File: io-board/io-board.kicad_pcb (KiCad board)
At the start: 2 copper layers, 82 x 64 mm, 101 parts, among them J1 Conn_01x03, J2 Conn_01x03, J3 Conn_01x03, J4 Conn_01x03, J5 Conn_01x24, K1 FRM18A-5 DC12V, K10 FRM18A-5 DC12V, K11 FRM18A-5 DC12V, K2 FRM18A-5 DC12V, K3 FRM18A-5 DC12V, K4 FRM18A-5 DC12V, K5 FRM18A-5 DC12V, K6 FRM18A-5 DC12V, K7 FRM18A-5 DC12V, K8 FRM18A-5 DC12V, K9 FRM18A-5 DC12V, Q1 NPN, Q10 NPN, Q11 NPN, Q2 NPN, Q3 NPN, Q4 NPN, Q5 NPN, Q6 NPN, Q7 NPN, Q8 NPN, Q9 NPN, U1 Littelfuse SP720, U2 Kamod BluePill STM32F103C8T6

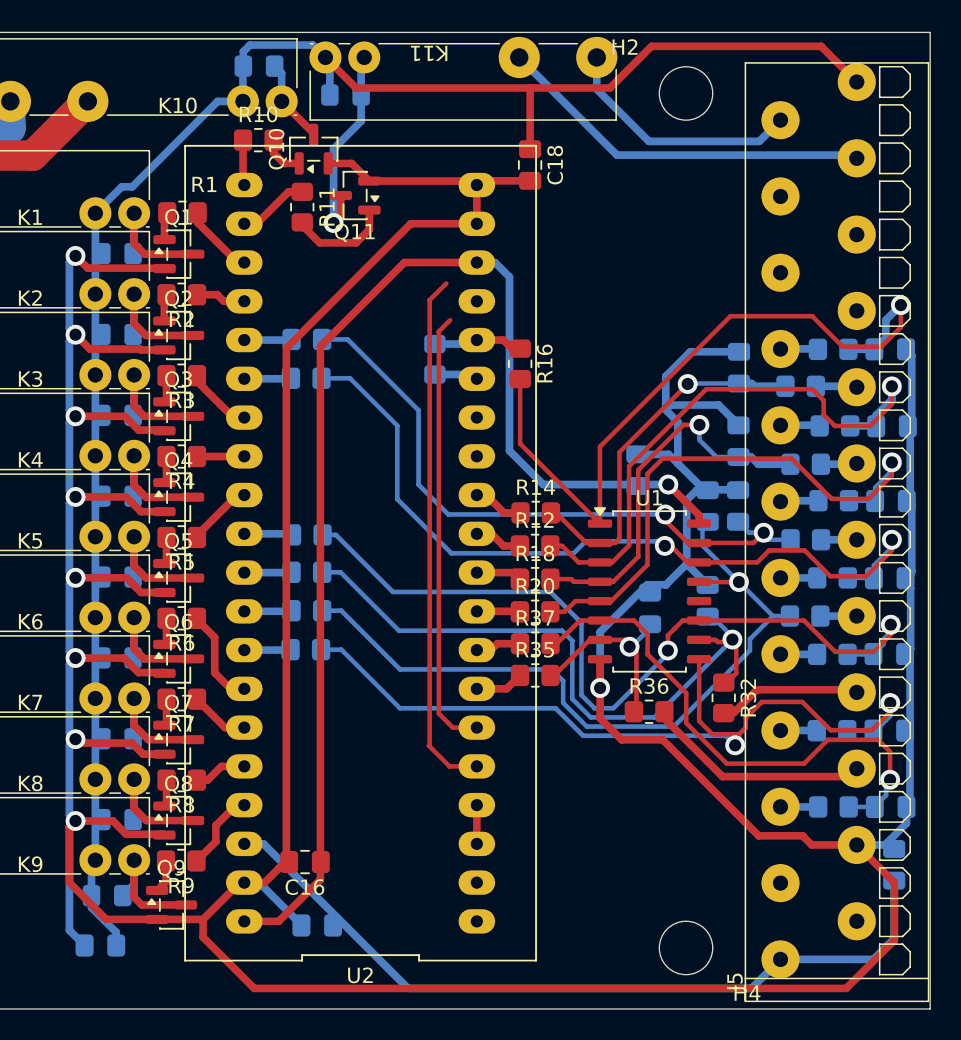
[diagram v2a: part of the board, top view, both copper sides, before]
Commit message: All added and connected in PCB. Cleanup needed.
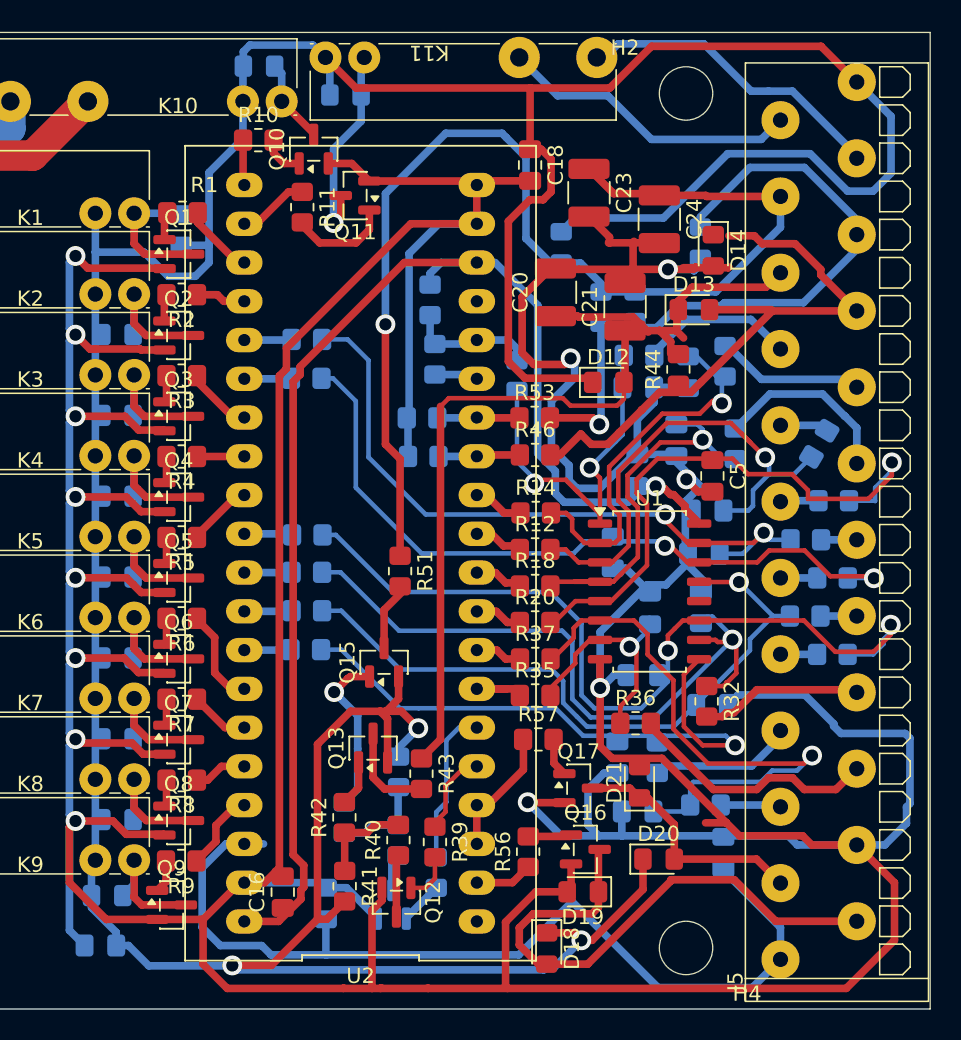
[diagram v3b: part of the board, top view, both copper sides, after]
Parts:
- added C20: C, Capacitor_SMD:C_1210_3225Metric_Pad1.33x2.70mm_HandSolder, F.Cu at (87.4, 47.0)
- added C21: C, Capacitor_SMD:C_1210_3225Metric_Pad1.33x2.70mm_HandSolder, F.Cu at (92.0, 48.0)
- added C23: C, Capacitor_SMD:C_1210_3225Metric_Pad1.33x2.70mm_HandSolder, F.Cu at (89.6, 40.5)
- added C24: C, Capacitor_SMD:C_1210_3225Metric_Pad1.33x2.70mm_HandSolder, F.Cu at (94.2, 42.2)
- added D12: D, Diode_SMD:D_0805_2012Metric_Pad1.15x1.40mm_HandSolder, F.Cu at (90.9, 52.9)
- added D13: D, Diode_SMD:D_0805_2012Metric_Pad1.15x1.40mm_HandSolder, F.Cu at (96.5, 48.2)
- added D14: D, Diode_SMD:D_0805_2012Metric_Pad1.15x1.40mm_HandSolder, F.Cu at (97.8, 44.3)
- added D15: D, Diode_SMD:D_0805_2012Metric_Pad1.15x1.40mm_HandSolder, B.Cu at (87.8, 44.1)
- added D16: D, Diode_SMD:D_0805_2012Metric_Pad1.15x1.40mm_HandSolder, B.Cu at (90.4, 48.0)
- added D17: D, Diode_SMD:D_0805_2012Metric_Pad1.15x1.40mm_HandSolder, B.Cu at (96.9, 43.8)
- added D18: D, Diode_SMD:D_0805_2012Metric_Pad1.15x1.40mm_HandSolder, F.Cu at (86.9, 90.0)
- added D19: D, Diode_SMD:D_0805_2012Metric_Pad1.15x1.40mm_HandSolder, F.Cu at (89.2, 86.3)
- added D20: D, Diode_SMD:D_0805_2012Metric_Pad1.15x1.40mm_HandSolder, F.Cu at (94.2, 84.2)
- added D21: D, Diode_SMD:D_0805_2012Metric_Pad1.15x1.40mm_HandSolder, F.Cu at (93.0, 79.1)
- added Q12: NPN, Package_TO_SOT_SMD:SOT-23, F.Cu at (77.0, 87.0)
- added Q13: PNP, Package_TO_SOT_SMD:SOT-23, F.Cu at (75.5, 76.9)
- added Q14: NPN, Package_TO_SOT_SMD:SOT-23, B.Cu at (76.7, 87.1)
- added Q15: PNP, Package_TO_SOT_SMD:SOT-23, F.Cu at (76.2, 71.3)
- added Q16: NPN, Package_TO_SOT_SMD:SOT-23, F.Cu at (89.4, 83.5)
- added Q17: NPN, Package_TO_SOT_SMD:SOT-23, F.Cu at (89.0, 79.5)
- added R39: R, Resistor_SMD:R_0805_2012Metric_Pad1.20x1.40mm_HandSolder, F.Cu at (79.5, 83.1)
- added R40: R, Resistor_SMD:R_0805_2012Metric_Pad1.20x1.40mm_HandSolder, F.Cu at (77.2, 82.9)
- added R41: R, Resistor_SMD:R_0805_2012Metric_Pad1.20x1.40mm_HandSolder, F.Cu at (73.6, 86.0)
- added R42: R, Resistor_SMD:R_0805_2012Metric_Pad1.20x1.40mm_HandSolder, F.Cu at (73.6, 81.4)
- added R43: R, Resistor_SMD:R_0805_2012Metric_Pad1.20x1.40mm_HandSolder, F.Cu at (78.7, 78.6)
- added R44: R, Resistor_SMD:R_0805_2012Metric_Pad1.20x1.40mm_HandSolder, F.Cu at (95.5, 52.1)
- added R45: R, Resistor_SMD:R_0805_2012Metric_Pad1.20x1.40mm_HandSolder, B.Cu at (78.8, 57.8)
- added R46: R, Resistor_SMD:R_0805_2012Metric_Pad1.20x1.40mm_HandSolder, F.Cu at (86.1, 57.7)
- added R47: R, Resistor_SMD:R_0805_2012Metric_Pad1.20x1.40mm_HandSolder, B.Cu at (79.6, 85.1)
- added R48: R, Resistor_SMD:R_0805_2012Metric_Pad1.20x1.40mm_HandSolder, B.Cu at (77.2, 78.5)
- added R49: R, Resistor_SMD:R_0805_2012Metric_Pad1.20x1.40mm_HandSolder, B.Cu at (77.1, 83.0)
- added R50: R, Resistor_SMD:R_0805_2012Metric_Pad1.20x1.40mm_HandSolder, B.Cu at (73.6, 81.5)
- added R51: R, Resistor_SMD:R_0805_2012Metric_Pad1.20x1.40mm_HandSolder, F.Cu at (77.3, 65.3)
- added R52: R, Resistor_SMD:R_0805_2012Metric_Pad1.20x1.40mm_HandSolder, B.Cu at (92.7, 48.0)
- added R53: R, Resistor_SMD:R_0805_2012Metric_Pad1.20x1.40mm_HandSolder, F.Cu at (86.1, 55.3)
- added R54: R, Resistor_SMD:R_0805_2012Metric_Pad1.20x1.40mm_HandSolder, B.Cu at (78.7, 55.3)
- added R55: 50K, Resistor_SMD:R_0805_2012Metric_Pad1.20x1.40mm_HandSolder, B.Cu at (79.2, 47.5)
- added R56: R, Resistor_SMD:R_0805_2012Metric_Pad1.20x1.40mm_HandSolder, F.Cu at (85.7, 83.7)
- added R57: R, Resistor_SMD:R_0805_2012Metric_Pad1.20x1.40mm_HandSolder, F.Cu at (86.3, 76.3)
- C5: moved to F.Cu
- R16: moved to B.Cu
- moved C7 18.2 mm to (91.2, 64.1), turned to -90 degrees
- moved C11 17.9 mm to (91.5, 77.5), turned to -90 degrees
- moved C1 16.7 mm to (92.9, 53.3)
- moved C13 16.6 mm to (92.8, 81.1), turned to 180 degrees
- moved C9 16.2 mm to (93.1, 72.1), turned to 180 degrees
- moved C3 13.3 mm to (97.4, 61.3), turned to 180 degrees
- moved C8 13.0 mm to (97.7, 74.1), turned to 0 degrees
- moved R17 12.7 mm to (92.9, 51.2), turned to 0 degrees
- moved C5 11.8 mm to (97.7, 59.1), turned to -90 degrees
- moved R34 11.6 mm to (94.1, 77.5), turned to -90 degrees
- moved C17 11.2 mm to (98.4, 83.8)
- moved R38 8.39 mm to (97.3, 80.6), turned to 0 degrees
- moved R15 5.21 mm to (98.6, 51.6), turned to 90 degrees
- moved R19 4.80 mm to (99.2, 57.0), turned to 90 degrees
- moved D1 4.46 mm to (62.9, 42.9), turned to 90 degrees
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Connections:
- net Net-(U2-Pin_3) renamed /OC2-IN
- J5 pad 18: /LED1-P -> /LED1-M
- J5 pad 19: /LED1-M -> /LED1-P
- J5 pad 20: /LED2-P -> /LED2-M
- J5 pad 21: /LED2-M -> /LED2-P
- J5 pad 22: REL11-OUT2 -> REL11-OUT1
- J5 pad 23: REL11-OUT1 -> REL11-OUT2
- U2 pad 13: unconnected-(U2-Pin_13-Pad13) -> /LED1-FB
- U2 pad 14: unconnected-(U2-Pin_14-Pad14) -> /LED2-FB
- U2 pad 2: unconnected-(U2-Pin_2-Pad2) -> /OC1-IN
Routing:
- net +12V: track 115.0 -> 257.8 mm, vias 0 -> 3
- net GND: track 350.6 -> 456.6 mm, vias 9 -> 13
- net /LED2-P: track 0.00 -> 75.9 mm, vias 0 -> 1
- net /LED1-P: track 0.00 -> 63.7 mm
- net /LED2-M: track 0.00 -> 45.6 mm, vias 0 -> 1
- net /LED1-M: track 0.00 -> 39.4 mm
- net /OC1: track 0.00 -> 36.8 mm
- net /LED1-PWM: track 34.5 -> 5.14 mm
- net /ESD1: track 48.1 -> 24.2 mm, vias 1 -> 2
- net /LED2-PWM: track 29.0 -> 10.3 mm
- net /OC2: track 0.00 -> 16.2 mm
- net /ESD8: track 54.8 -> 38.8 mm, vias 2 -> 1
- net Net-(Q15-B): track 0.00 -> 11.0 mm, vias 0 -> 1
- net +5V: track 51.7 -> 61.6 mm
- net /IO3: track 2.37 -> 12.2 mm
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
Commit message: PCB: All component locations done
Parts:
- moved K11 18.4 mm to (90.6, 34.5), turned to 0 degrees
- moved D11 13.1 mm to (86.4, 37.2), turned to 180 degrees
- moved C17 11.5 mm to (87.0, 85.3)
- moved C16 7.69 mm to (63.0, 90.3), turned to 180 degrees
- moved D19 6.64 mm to (84.8, 91.2)
- moved Q11 6.41 mm to (75.5, 47.0)
- moved Q10 6.39 mm to (76.9, 41.2)
- moved R11 6.33 mm to (70.7, 47.8)
- moved C14 6.03 mm to (87.2, 56.4), turned to 0 degrees
- moved R33 5.13 mm to (71.5, 75.6)
- moved D10 5.06 mm to (68.3, 37.3)
- moved R51 4.91 mm to (73.9, 61.7)
- moved D3 4.91 mm to (63.3, 53.2), turned to 90 degrees
- moved D2 4.87 mm to (63.3, 48.1), turned to -90 degrees
- moved D4 4.86 mm to (63.3, 58.7), turned to 90 degrees
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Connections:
- U2 pad 22: REL11-IN -> REL1-IN
- U2 pad 23: REL1-IN -> REL11-IN
- U2 pad 26: /IO-IN6 -> REL3-IN
- U2 pad 27: REL3-IN -> /IO-IN6
- U2 pad 29: REL5-IN -> /IO-IN8
- U2 pad 30: /IO-IN8 -> REL5-IN
- U2 pad 32: /IO-IN7 -> REL6-IN
- U2 pad 33: /IO-IN10 -> /IO-IN7
- U2 pad 34: REL6-IN -> REL7-IN
- U2 pad 35: REL7-IN -> /IO-IN10
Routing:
- net +12V: track 257.8 -> 275.8 mm
- net REL11-OUT1: track 21.3 -> 39.0 mm
- net Net-(D11-A): track 13.7 -> 26.7 mm
- net REL11-OUT2: track 19.9 -> 30.7 mm
- net Net-(D10-A): track 5.56 -> 13.6 mm
- net Net-(R40-Pad2): track 6.27 -> 13.0 mm
- net /LED2-M: track 45.6 -> 51.4 mm
- net +5V: track 61.6 -> 56.2 mm
- net /ESD13: track 47.4 -> 43.3 mm
- net /ESD8: track 38.8 -> 42.8 mm
- net /ESD9: track 44.9 -> 41.0 mm
- net /ESD12: track 43.9 -> 40.7 mm
- net REL6-IN: track 6.43 -> 3.29 mm
- net /LED1-P: track 63.7 -> 60.6 mm
- net Net-(Q9-B): track 2.17 -> 5.01 mm
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
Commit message: PCB: All in place, need to prepare for production
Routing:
- net GND: track 456.9 -> 475.9 mm, vias 13 -> 14
- net /ESD5: track 38.7 -> 32.8 mm
- net /LED2-P: track 75.4 -> 80.3 mm
- net /ESD10: track 53.3 -> 48.7 mm
- net /LED1-P: track 60.6 -> 63.5 mm
- net /ESD13: track 43.3 -> 44.9 mm
- net /ESD3: track 32.4 -> 31.1 mm
- net /IO11: track 16.3 -> 15.1 mm
- net /ESD6: track 37.8 -> 39.1 mm
- net REL9-IN: track 5.27 -> 5.89 mm
- added copper zone on B.Cu, net GND
- added copper zone on F.Cu, net GND

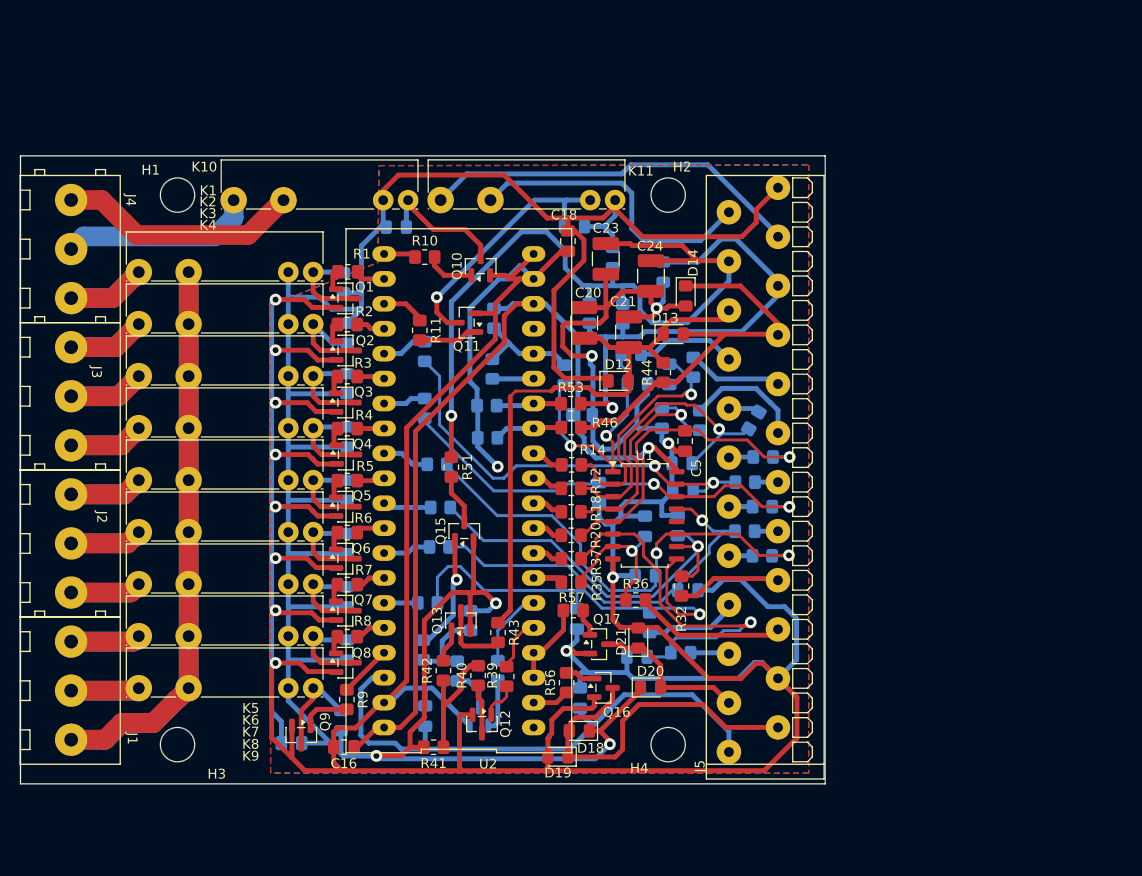
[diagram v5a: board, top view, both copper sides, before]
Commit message: PCB: Stencil holders and production configuration
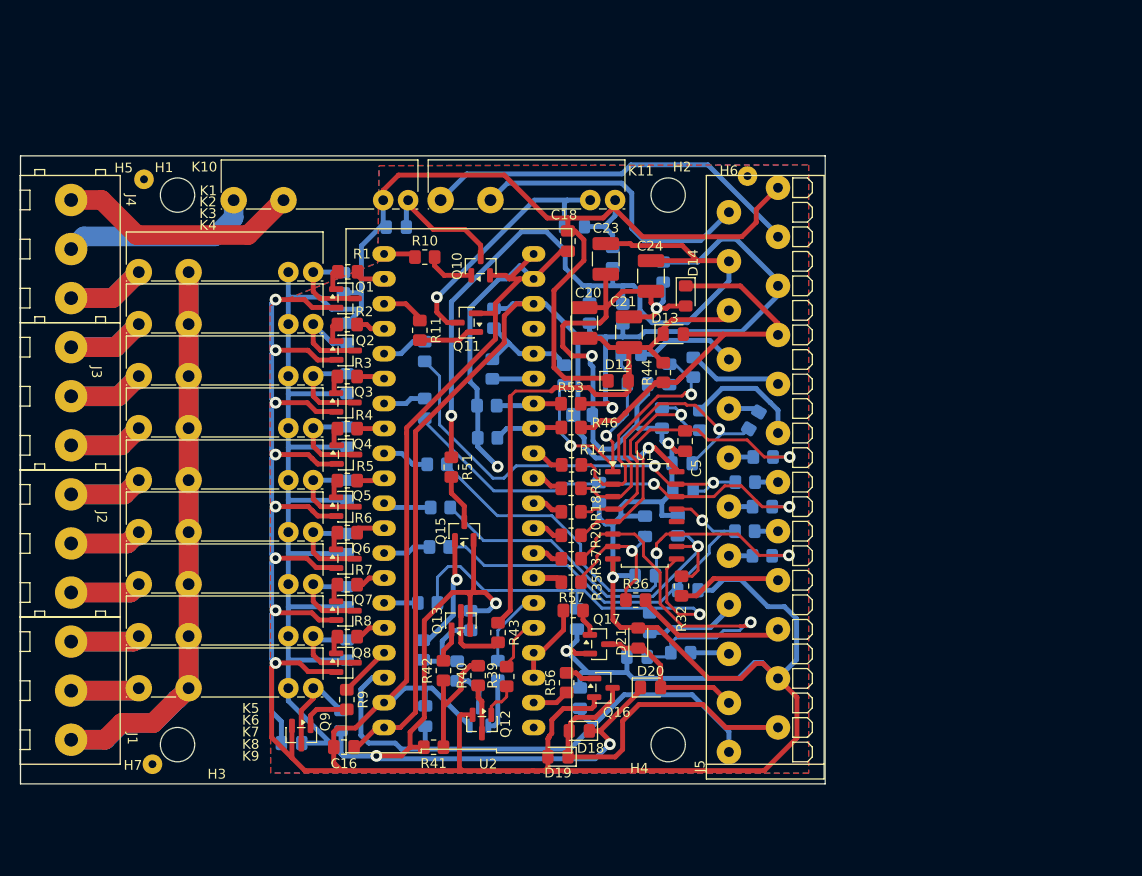
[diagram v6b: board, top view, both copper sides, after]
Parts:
- added H5: Conn_01x01, Footprints:stencil-holder, F.Cu at (42.6, 32.4)
- added H6: Conn_01x01, Footprints:stencil-holder, F.Cu at (104.1, 32.1)
- added H7: Conn_01x01, Footprints:stencil-holder, F.Cu at (43.4, 92.0)
